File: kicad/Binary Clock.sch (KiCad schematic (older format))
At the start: 53 parts, among them J1 AVR-ISP-10, SW1 INC_HOUR, SW2 INC_MINUTE, SW3 INC_SECOND, U1 ATmega32A-PU, U2 PCF8583P, Y1 32768hZ

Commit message: Add INC_BTNESS button to schema
INC_BTNESS button is desired to increment LED display brightness
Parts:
- removed R11, R12, R4: 10k, Resistor_SMD:R_1206_3216Metric_Pad1.30x1.75mm_HandSolder, symbol Device:R
- added SW4: INC_BTNESS, Button_Switch_THT:SW_PUSH_6mm, symbol Switch:SW_Push
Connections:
- net labels added: INC_BTNESS
- wire segments 207 -> 204
- no-connect marks 17 -> 16
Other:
- moved on the sheet: SW1, SW2, SW3
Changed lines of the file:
@@
 L Switch:SW_Push SW1
 U 1 1 5FCC0002
-P 7950 5650
-F 0 "SW1" V 7904 5798 50  0000 L CNN
-F 1 "INC_HOUR" V 7995 5798 50  0000 L CNN
-F 2 "Button_Switch_THT:SW_PUSH_6mm" H 7950 5850 50  0001 C CNN
-F 3 "~" H 7950 5850 50  0001 C CNN
-	1    7950 5650
+P 7650 5400
+F 0 "SW1" V 7604 5548 50  0000 L CNN
+F 1 "INC_HOUR" V 7695 5548 50  0000 L CNN
+F 2 "Button_Switch_THT:SW_PUSH_6mm" H 7650 5600 50  0001 C CNN
+F 3 "~" H 7650 5600 50  0001 C CNN
+	1    7650 5400
 	0    1    1    0
 $EndComp
 Wire Wire Line
-	7950 5850 7950 5900
+	7650 5600 7650 5650
 $Comp
 L power:GND #PWR?
 U 1 1 5FCC8117
-P 7950 5900
-F 0 "#PWR?" H 7950 5650 50  0001 C CNN
-F 1 "GND" H 7955 5727 50  0000 C CNN
-F 2 "" H 7950 5900 50  0001 C CNN
-F 3 "" H 7950 5900 50  0001 C CNN
-	1    7950 5900
-	1    0    0    -1
-$EndComp
-Wire Wire Line
-	7950 5450 7950 5350
-Wire Wire Line
-	7550 5350 7950 5350
-Text Label 7550 5350 0    39   ~ 0
-INC_HOUR
-$Comp
-L Device:R R4
-U 1 1 5FCEA36D
-P 7950 5100
-F 0 "R4" H 8020 5146 50  0000 L CNN
-F 1 "10k" H 8020 5055 50  0000 L CNN
-F 2 "Resistor_SMD:R_1206_3216Metric_Pad1.30x1.75mm_HandSolder" V 7880 5100 50  0001 C CNN
-F 3 "~" H 7950 5100 50  0001 C CNN
-	1    7950 5100
-	1    0    0    -1
-$EndComp
-Wire Wire Line
-	7950 5350 7950 5250
-Connection ~ 7950 5350
-Wire Wire Line
-	7950 4950 7950 4900
-$Comp
-L power:VCC #PWR?
-U 1 1 5FCCF855
-P 7950 4900
-F 0 "#PWR?" H 7950 4750 50  0001 C CNN
-F 1 "VCC" H 7965 5073 50  0000 C CNN
-F 2 "" H 7950 4900 50  0001 C CNN
-F 3 "" H 7950 4900 50  0001 C CNN
-	1    7950 4900
+P 7650 5650
+F 0 "#PWR?" H 7650 5400 50  0001 C CNN
+F 1 "GND" H 7655 5477 50  0000 C CNN
+F 2 "" H 7650 5650 50  0001 C CNN
+F 3 "" H 7650 5650 50  0001 C CNN
+	1    7650 5650
 	1    0    0    -1
 $EndComp
@@
 L Switch:SW_Push SW2
 U 1 1 5FD056CB
-P 9100 5650
-F 0 "SW2" V 9054 5798 50  0000 L CNN
-F 1 "INC_MINUTE" V 9145 5798 50  0000 L CNN
-F 2 "Button_Switch_THT:SW_PUSH_6mm" H 9100 5850 50  0001 C CNN
-F 3 "~" H 9100 5850 50  0001 C CNN
-	1    9100 5650
+P 8550 5400
+F 0 "SW2" V 8504 5548 50  0000 L CNN
+F 1 "INC_MINUTE" V 8595 5548 50  0000 L CNN
+F 2 "Button_Switch_THT:SW_PUSH_6mm" H 8550 5600 50  0001 C CNN
+F 3 "~" H 8550 5600 50  0001 C CNN
+	1    8550 5400
 	0    1    1    0
 $EndComp
 Wire Wire Line
-	9100 5850 9100 5900
+	8550 5600 8550 5650
 $Comp
 L power:GND #PWR?
 U 1 1 5FD056E8
-P 9100 5900
-F 0 "#PWR?" H 9100 5650 50  0001 C CNN
-F 1 "GND" H 9105 5727 50  0000 C CNN
-F 2 "" H 9100 5900 50  0001 C CNN
-F 3 "" H 9100 5900 50  0001 C CNN
-	1    9100 5900
-	1    0    0    -1
-$EndComp
-Wire Wire Line
-	9100 5450 9100 5350
-Wire Wire Line
-	8700 5350 9100 5350
-Text Label 8700 5350 0    39   ~ 0
-INC_MINUTE
-$Comp
-L Device:R R11
-U 1 1 5FD056F5
-P 9100 5100
-F 0 "R11" H 9170 5146 50  0000 L CNN
-F 1 "10k" H 9170 5055 50  0000 L CNN
-F 2 "Resistor_SMD:R_1206_3216Metric_Pad1.30x1.75mm_HandSolder" V 9030 5100 50  0001 C CNN
-F 3 "~" H 9100 5100 50  0001 C CNN
-	1    9100 5100
-	1    0    0    -1
-$EndComp
-Wire Wire Line
-	9100 5350 9100 5250
-Connection ~ 9100 5350
-Wire Wire Line
-	9100 4950 9100 4900
-$Comp
-L power:VCC #PWR?
-U 1 1 5FD05702
-P 9100 4900
-F 0 "#PWR?" H 9100 4750 50  0001 C CNN
-F 1 "VCC" H 9115 5073 50  0000 C CNN
-F 2 "" H 9100 4900 50  0001 C CNN
-F 3 "" H 9100 4900 50  0001 C CNN
-	1    9100 4900
+P 8550 5650
+F 0 "#PWR?" H 8550 5400 50  0001 C CNN
+F 1 "GND" H 8555 5477 50  0000 C CNN
+F 2 "" H 8550 5650 50  0001 C CNN
+F 3 "" H 8550 5650 50  0001 C CNN
+	1    8550 5650
 	1    0    0    -1
 $EndComp
@@
 L Switch:SW_Push SW3
 U 1 1 5FD0D6D9
-P 10100 5650
-F 0 "SW3" V 10054 5798 50  0000 L CNN
-F 1 "INC_SECOND" V 10145 5798 50  0000 L CNN
-F 2 "Button_Switch_THT:SW_PUSH_6mm" H 10100 5850 50  0001 C CNN
-F 3 "~" H 10100 5850 50  0001 C CNN
-	1    10100 5650
+P 9450 5400
+F 0 "SW3" V 9404 5548 50  0000 L CNN
+F 1 "INC_SECOND" V 9495 5548 50  0000 L CNN
+F 2 "Button_Switch_THT:SW_PUSH_6mm" H 9450 5600 50  0001 C CNN
+F 3 "~" H 9450 5600 50  0001 C CNN
+	1    9450 5400
 	0    1    1    0
 $EndComp
 Wire Wire Line
-	10100 5850 10100 5900
+	9450 5600 9450 5650
 $Comp
 L power:GND #PWR?
 U 1 1 5FD0D6F6
-P 10100 5900
-F 0 "#PWR?" H 10100 5650 50  0001 C CNN
-F 1 "GND" H 10105 5727 50  0000 C CNN
-F 2 "" H 10100 5900 50  0001 C CNN
-F 3 "" H 10100 5900 50  0001 C CNN
-	1    10100 5900
-	1    0    0    -1
-$EndComp
-Wire Wire Line
-	10100 5450 10100 5350
-Wire Wire Line
-	9700 5350 10100 5350
-Text Label 9700 5350 0    39   ~ 0
-INC_SECOND
-$Comp
-L Device:R R12
-U 1 1 5FD0D703
-P 10100 5100
-F 0 "R12" H 10170 5146 50  0000 L CNN
-F 1 "10k" H 10170 5055 50  0000 L CNN
-F 2 "Resistor_SMD:R_1206_3216Metric_Pad1.30x1.75mm_HandSolder" V 10030 5100 50  0001 C CNN
-F 3 "~" H 10100 5100 50  0001 C CNN
-	1    10100 5100
-	1    0    0    -1
-$EndComp
-Wire Wire Line
-	10100 5350 10100 5250
-Connection ~ 10100 5350
-Wire Wire Line
-	10100 4950 10100 4900
-$Comp
-L power:VCC #PWR?
-U 1 1 5FD0D710
-P 10100 4900
-F 0 "#PWR?" H 10100 4750 50  0001 C CNN
-F 1 "VCC" H 10115 5073 50  0000 C CNN
-F 2 "" H 10100 4900 50  0001 C CNN
-F 3 "" H 10100 4900 50  0001 C CNN
-	1    10100 4900
+P 9450 5650
+F 0 "#PWR?" H 9450 5400 50  0001 C CNN
+F 1 "GND" H 9455 5477 50  0000 C CNN
+F 2 "" H 9450 5650 50  0001 C CNN
+F 3 "" H 9450 5650 50  0001 C CNN
+	1    9450 5650
 	1    0    0    -1
 $EndComp
@@
 	3000 3250 3100 3250
 Wire Wire Line
-	3000 2450 3100 2450
-Wire Wire Line
 	3000 2550 3100 2550
 Wire Wire Line
@@
 NoConn ~ 3100 1850
 NoConn ~ 3100 1950
-NoConn ~ 3100 2450
 NoConn ~ 3100 2550
 NoConn ~ 3100 3250
@@
 Text Label 5800 1500 0    39   ~ 0
 HOUR_LED
+Text Label 7250 5100 0    39   ~ 0
+INC_HOUR
+Wire Wire Line
+	7250 5100 7650 5100
+Wire Wire Line
+	7650 5200 7650 5100
+Text Label 8150 5100 0    39   ~ 0
+INC_MINUTE
+Wire Wire Line
+	8150 5100 8550 5100
+Wire Wire Line
+	8550 5200 8550 5100
+Text Label 9050 5100 0    39   ~ 0
+INC_SECOND
+Wire Wire Line
+	9050 5100 9450 5100
+Wire Wire Line
+	9450 5200 9450 5100
+$Comp
+L Switch:SW_Push SW4
+U 1 1 5FD20DE5
+P 10350 5400
+F 0 "SW4" V 10304 5548 50  0000 L CNN
+F 1 "INC_BTNESS" V 10395 5548 50  0000 L CNN
+F 2 "Button_Switch_THT:SW_PUSH_6mm" H 10350 5600 50  0001 C CNN
+F 3 "~" H 10350 5600 50  0001 C CNN
+	1    10350 5400
+	0    1    1    0
+$EndComp
+Wire Wire Line
+	10350 5600 10350 5650
+$Comp
+L power:GND #PWR?
+U 1 1 5FD20E02
+P 10350 5650
+F 0 "#PWR?" H 10350 5400 50  0001 C CNN
+F 1 "GND" H 10355 5477 50  0000 C CNN
+F 2 "" H 10350 5650 50  0001 C CNN
+F 3 "" H 10350 5650 50  0001 C CNN
+	1    10350 5650
+	1    0    0    -1
+$EndComp
+Text Label 9950 5100 0    39   ~ 0
+INC_BTNESS
+Wire Wire Line
+	9950 5100 10350 5100
+Wire Wire Line
+	10350 5200 10350 5100
+Wire Wire Line
+	3000 2450 3400 2450
+Text Label 3400 2450 2    39   ~ 0
+INC_BTNESS
 $EndSCHEMATC

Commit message: Update schema and PCB design
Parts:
- added J2: UART, Connector_PinHeader_1.27mm:PinHeader_1x04_P1.27mm_Vertical, symbol Connector_Generic:Conn_01x04
- added J3: COM/TWI, Connector_PinHeader_1.27mm:PinHeader_1x10_P1.27mm_Vertical, symbol Connector_Generic:Conn_01x10
- renumbered C10 to C2, C2 to C3, C3 to C4, C4 to C5, C5 to C6, C8 to C7, C9 to C8, HD0 to HD1, HD1 to HD2, HD2 to HD3, HD3 to HD4, HD4 to HD5, JP3 to JP1, MD0 to MD1, MD1 to MD2, MD2 to MD3, MD3 to MD4, MD4 to MD5, MD5 to MD6, R13 to R10, R14 to R11, R15 to R12, R5 to R4, R6 to R5, R7 to R6, R8 to R7, R9 to R8, R10 to R9, SD0 to SD1, SD1 to SD2, SD2 to SD3, SD3 to SD4, SD4 to SD5, SD5 to SD6, U2 to U1, U1 to U2
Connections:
- net labels added: COM0, COM1, COM2, COM3, COM4, COM5, RX, TX
- wire segments 204 -> 222
- no-connect marks 16 -> 8
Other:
- moved on the sheet: SW1, SW2, SW3, SW4

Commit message: Update schema and PCB design
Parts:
- removed JP1: S_EN, Connector_PinHeader_1.27mm:PinHeader_1x02_P1.27mm_Vertical, symbol Device:Jumper_NO_Small
- added JP1: TWI_ADDR, Connector_PinHeader_1.27mm:PinHeader_1x03_P1.27mm_Horizontal, symbol Jumper:Jumper_3_Open
- added JP2: S_EN, Connector_PinHeader_1.27mm:PinHeader_1x02_P1.27mm_Vertical, symbol Jumper:Jumper_2_Open
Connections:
- wire segments 222 -> 226
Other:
- moved on the sheet: C2, C4, C5, C6, D1, U1, Y1

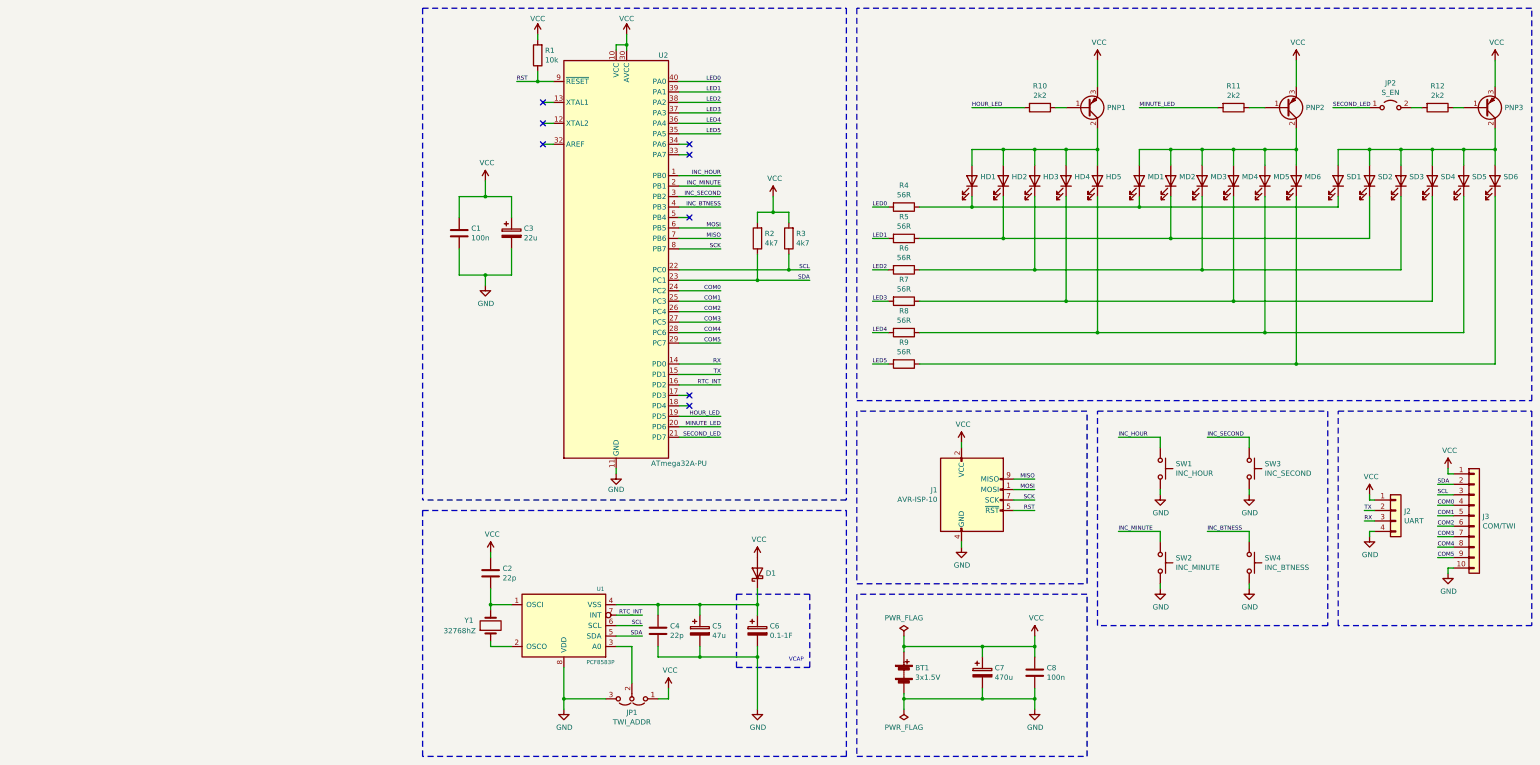
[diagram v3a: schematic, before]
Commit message: Add support for buzzer
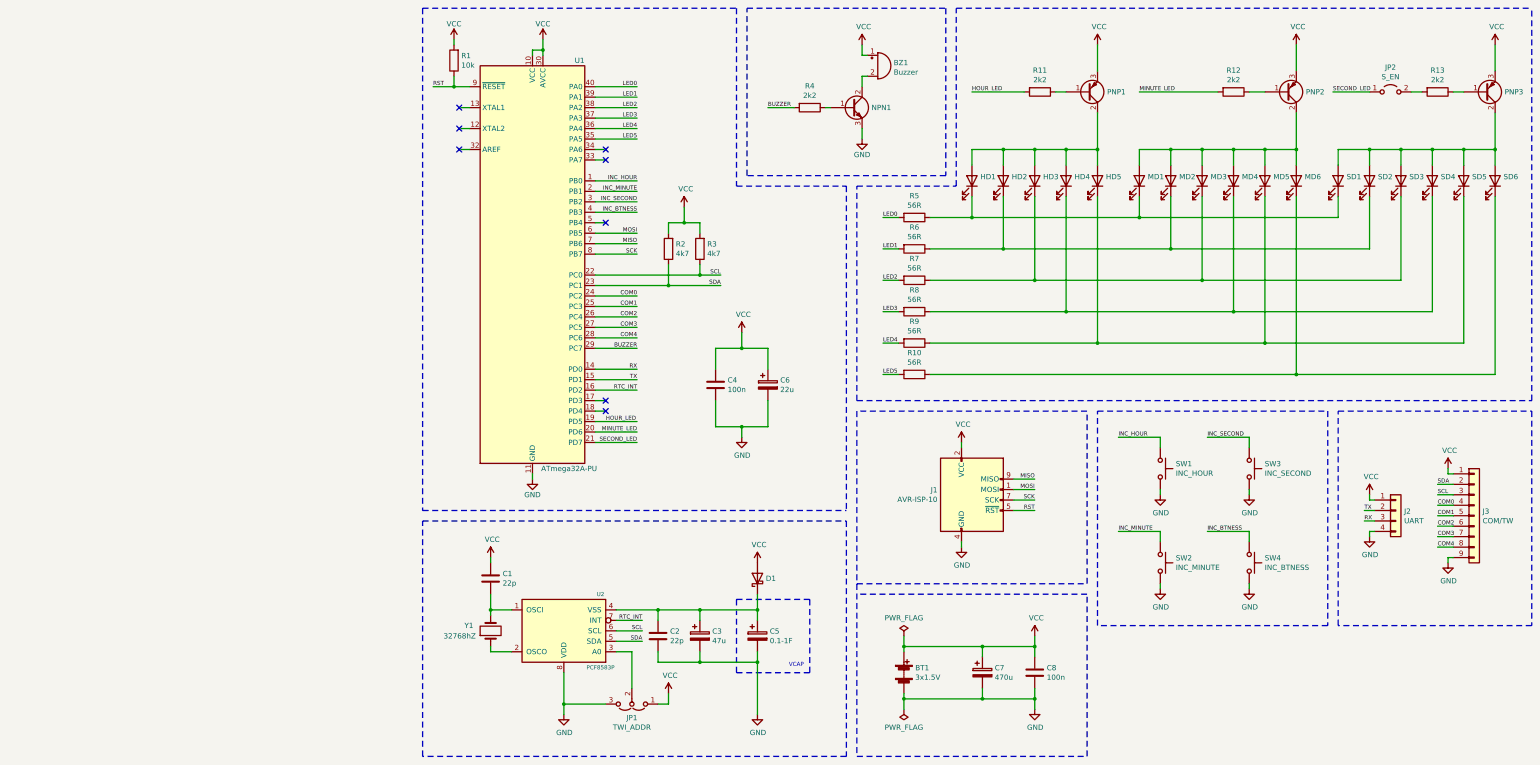
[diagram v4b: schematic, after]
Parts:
- removed J3: COM/TWI, Connector_PinHeader_1.27mm:PinHeader_1x10_P1.27mm_Vertical, symbol Connector_Generic:Conn_01x10
- added BZ1: Buzzer, Buzzer_Beeper:Buzzer_12x9.5RM7.6, symbol Device:Buzzer
- added J3: COM/TW, Connector_PinHeader_1.27mm:PinHeader_1x09_P1.27mm_Vertical, symbol Connector_Generic:Conn_01x09
- added NPN1: Q_NPN_BCE, Package_TO_SOT_SMD:SOT-223, symbol Device:Q_NPN_BCE
- added R4: 2k2, Resistor_SMD:R_1206_3216Metric_Pad1.30x1.75mm_HandSolder, symbol Device:R
- renumbered C2 to C1, C4 to C2, C5 to C3, C1 to C4, C6 to C5, C3 to C6, R9 to R10, R10 to R11, R11 to R12, R12 to R13, R4 to R5, R5 to R6, R6 to R7, R7 to R8, R8 to R9, U2 to U1, U1 to U2
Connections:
- net COM0: now also J3.4 (Pin_4)
- net COM1: now also J3.5 (Pin_5)
- net COM2: now also J3.6 (Pin_6)
- net COM3: now also J3.7 (Pin_7)
- net COM4: now also J3.8 (Pin_8)
- net GND: now also J3.9 (Pin_9), NPN1.3 (E)
- net SCL: now also J3.3 (Pin_3)
- net SDA: now also J3.2 (Pin_2)
- net VCC: now also BZ1.1 (-), J3.1 (Pin_1)
- net COM5 renamed BUZZER
- net BUZZER: now also R4.2
- new net: BZ1.2 (+), NPN1.2 (C)
- new net: NPN1.1 (B), R4.1
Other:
- moved on the sheet: C1, C2, C3, C4, C5, C6, D1, JP1, JP2, PNP1, PNP2, PNP3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

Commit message: Change goldpins to 2.56mm
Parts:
- D1: footprint Diode_SMD:D_SOD-523 -> Diode_SMD:D_2114_3652Metric
- J2: footprint Connector_PinHeader_1.27mm:PinHeader_1x04_P1.27mm_Vertical -> Connector_PinHeader_2.54mm:PinHeader_1x04_P2.54mm_Vertical
- J3: footprint Connector_PinHeader_1.27mm:PinHeader_1x09_P1.27mm_Vertical -> Connector_PinHeader_2.54mm:PinHeader_1x09_P2.54mm_Vertical
- JP1: footprint Connector_PinHeader_1.27mm:PinHeader_1x03_P1.27mm_Horizontal -> Connector_PinHeader_2.54mm:PinHeader_1x03_P2.54mm_Horizontal
- JP2: footprint Connector_PinHeader_1.27mm:PinHeader_1x02_P1.27mm_Vertical -> Connector_PinHeader_2.54mm:PinHeader_1x02_P2.54mm_Vertical
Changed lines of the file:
@@
 F 0 "J2" H 9930 5342 50  0000 L CNN
 F 1 "UART" H 9930 5251 50  0000 L CNN
-F 2 "Connector_PinHeader_1.27mm:PinHeader_1x04_P1.27mm_Vertical" H 9850 5350 50  0001 C CNN
+F 2 "Connector_PinHeader_2.54mm:PinHeader_1x04_P2.54mm_Vertical" H 9850 5350 50  0001 C CNN
 F 3 "~" H 9850 5350 50  0001 C CNN
 	1    9850 5350
@@
 F 0 "D1" V 3750 5920 50  0000 R CNN
 F 1 "D_Schottky" V 3705 5920 50  0001 R CNN
-F 2 "Diode_SMD:D_SOD-523" H 3750 6000 50  0001 C CNN
+F 2 "Diode_SMD:D_2114_3652Metric" H 3750 6000 50  0001 C CNN
 F 3 "~" H 3750 6000 50  0001 C CNN
 	1    3750 6000
@@
 F 0 "JP1" H 2550 7331 50  0000 C CNN
 F 1 "TWI_ADDR" H 2550 7422 50  0000 C CNN
-F 2 "Connector_PinHeader_1.27mm:PinHeader_1x03_P1.27mm_Horizontal" H 2550 7200 50  0001 C CNN
+F 2 "Connector_PinHeader_2.54mm:PinHeader_1x03_P2.54mm_Horizontal" H 2550 7200 50  0001 C CNN
 F 3 "~" H 2550 7200 50  0001 C CNN
 	1    2550 7200
@@
 F 0 "JP2" H 9800 1585 50  0000 C CNN
 F 1 "S_EN" H 9800 1494 50  0000 C CNN
-F 2 "Connector_PinHeader_1.27mm:PinHeader_1x02_P1.27mm_Vertical" H 9800 1350 50  0001 C CNN
+F 2 "Connector_PinHeader_2.54mm:PinHeader_1x02_P2.54mm_Vertical" H 9800 1350 50  0001 C CNN
 F 3 "~" H 9800 1350 50  0001 C CNN
 	1    9800 1350
@@
 F 0 "J3" H 10680 5442 50  0000 L CNN
 F 1 "COM/TW" H 10680 5351 50  0000 L CNN
-F 2 "Connector_PinHeader_1.27mm:PinHeader_1x09_P1.27mm_Vertical" H 10600 5400 50  0001 C CNN
+F 2 "Connector_PinHeader_2.54mm:PinHeader_1x09_P2.54mm_Vertical" H 10600 5400 50  0001 C CNN
 F 3 "~" H 10600 5400 50  0001 C CNN
 	1    10600 5400

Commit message: Update PCB footprints
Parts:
- BT1: footprint Battery:BatteryHolder_TruPower_BH-331P_3xAA -> Project Footprints:BatteryPackage
- C5: footprint Capacitor_THT:C_Disc_D12.5mm_W5.0mm_P10.00mm -> Project Footprints:SuperCapacitor
- C6: footprint Capacitor_SMD:CP_Elec_6.3x5.3 -> Capacitor_SMD:CP_Elec_4x3
- NPN1, PNP1, PNP2, PNP3: footprint Package_TO_SOT_SMD:SOT-223 -> Package_TO_SOT_SMD:SOT-23
- U2: footprint Package_SO:Diodes_SO-8EP -> PCF8583:SOT176-1
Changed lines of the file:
@@
 F 0 "C6" H 3968 4196 50  0000 L CNN
 F 1 "22u" H 3968 4105 50  0000 L CNN
-F 2 "Capacitor_SMD:CP_Elec_6.3x5.3" H 3888 4000 50  0001 C CNN
+F 2 "Capacitor_SMD:CP_Elec_4x3" H 3888 4000 50  0001 C CNN
 F 3 "~" H 3850 4150 50  0001 C CNN
 	1    3850 4150
@@
 F 0 "BT1" H 5258 6946 50  0000 L CNN
 F 1 "3x1.5V" H 5258 6855 50  0000 L CNN
-F 2 "Battery:BatteryHolder_TruPower_BH-331P_3xAA" V 5150 6960 50  0001 C CNN
+F 2 "Project Footprints:BatteryPackage" V 5150 6960 50  0001 C CNN
 F 3 "~" V 5150 6960 50  0001 C CNN
 	1    5150 6900
@@
 F 0 "PNP3" H 10891 1350 50  0000 L CNN
 F 1 "Q_PNP_BCE" H 10890 1395 50  0001 L CNN
-F 2 "Package_TO_SOT_SMD:SOT-223" H 10900 1450 50  0001 C CNN
+F 2 "Package_TO_SOT_SMD:SOT-23" H 10900 1450 50  0001 C CNN
 F 3 "~" H 10700 1350 50  0001 C CNN
 	1    10700 1350
@@
 F 0 "PNP2" H 8991 1350 50  0000 L CNN
 F 1 "Q_PNP_BCE" H 8990 1395 50  0001 L CNN
-F 2 "Package_TO_SOT_SMD:SOT-223" H 9000 1450 50  0001 C CNN
+F 2 "Package_TO_SOT_SMD:SOT-23" H 9000 1450 50  0001 C CNN
 F 3 "~" H 8800 1350 50  0001 C CNN
 	1    8800 1350
@@
 F 0 "PNP1" H 7091 1350 50  0000 L CNN
 F 1 "Q_PNP_BCE" H 7090 1395 50  0001 L CNN
-F 2 "Package_TO_SOT_SMD:SOT-223" H 7100 1450 50  0001 C CNN
+F 2 "Package_TO_SOT_SMD:SOT-23" H 7100 1450 50  0001 C CNN
 F 3 "~" H 6900 1350 50  0001 C CNN
 	1    6900 1350
@@
 F 0 "U2" H 2250 6050 39  0000 C CNN
 F 1 "PCF8583P" H 2250 5350 39  0000 C CNN
-F 2 "Package_SO:Diodes_SO-8EP" H 1900 6100 39  0001 C CNN
+F 2 "PCF8583:SOT176-1" H 1900 6100 39  0001 C CNN
 F 3 "" H 1900 6100 39  0001 C CNN
 	1    1900 6100
@@
 F 0 "C5" H 3868 6596 50  0000 L CNN
 F 1 "0.1-1F" H 3868 6505 50  0000 L CNN
-F 2 "Capacitor_THT:C_Disc_D12.5mm_W5.0mm_P10.00mm" H 3788 6400 50  0001 C CNN
+F 2 "Project Footprints:SuperCapacitor" H 3788 6400 50  0001 C CNN
 F 3 "~" H 3750 6550 50  0001 C CNN
 	1    3750 6550
@@
 F 0 "NPN1" H 4840 1500 50  0000 L CNN
 F 1 "Q_NPN_BCE" H 4841 1455 50  0001 L CNN
-F 2 "Package_TO_SOT_SMD:SOT-223" H 4850 1600 50  0001 C CNN
+F 2 "Package_TO_SOT_SMD:SOT-23" H 4850 1600 50  0001 C CNN
 F 3 "~" H 4650 1500 50  0001 C CNN
 	1    4650 1500
